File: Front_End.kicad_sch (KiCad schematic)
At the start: 40 parts, among them J6 Conn_01x03, J7 Conn_01x03, J8 Conn_01x03, J9 Conn_01x03

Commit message: Bring over ringof/dev (tranche 2, stage 1): design, library, 3D, board CI & docs
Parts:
- C48, C49, C50, C53, C54, C55, C56, C58, C59, C61: footprint TIS_Footprints:C_0603 -> Library:C_0603
- C51, C52, C57, C60: footprint TIS_Footprints:PAD_0603 -> Library:C_0603
- J6, J7, J8, J9: footprint TIS_Footprints:Pin_Header_Straight_1x03_Pitch2.54mm -> Library:Pin_Header_Straight_1x03_Pitch2.54mm
- L10, L11, L12, L13, L14, L8, L9: footprint TIS_Footprints:Murata2U -> Library:Murata2U
- R28, R29, R30, R31, R32, R33, R34, R35, R36, R37, R38, R39, R40: footprint TIS_Footprints:PAD_0603 -> Library:PAD_0603
- U12, U13: footprint TIS_Footprints:SOT-23 -> Library:SOT-23
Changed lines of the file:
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@@
 			)
 		)
-		(property "Footprint" "TIS_Footprints:PAD_0603"
+		(property "Footprint" "Library:PAD_0603"
 			(at 117.856 65.024 90)
 			(hide yes)
@@
 			)
 		)
-		(property "Footprint" "TIS_Footprints:PAD_0603"
+		(property "Footprint" "Library:C_0603"
 			(at 60.96 99.06 0)
 			(hide yes)
@@
 			)
 		)
-		(property "Footprint" "TIS_Footprints:Pin_Header_Straight_1x03_Pitch2.54mm"
+		(property "Footprint" "Library:Pin_Header_Straight_1x03_Pitch2.54mm"
 			(at 51.181 21.336 0)
 			(hide yes)
@@
 			)
 		)
-		(property "Footprint" "TIS_Footprints:PAD_0603"
+		(property "Footprint" "Library:PAD_0603"
 			(at 77.216 65.024 90)
 			(hide yes)
@@
 			)
 		)
-		(property "Footprint" "TIS_Footprints:C_0603"
+		(property "Footprint" "Library:C_0603"
 			(at 96.774 135.382 0)
 			(hide yes)
@@
 			)
 		)
-		(property "Footprint" "TIS_Footprints:Murata2U"
+		(property "Footprint" "Library:Murata2U"
 			(at 64.77 111.76 0)
 			(hide yes)
@@
 			)
 		)
-		(property "Footprint" "TIS_Footprints:Murata2U"
+		(property "Footprint" "Library:Murata2U"
 			(at 170.18 111.76 0)
 			(hide yes)
@@
 			)
 		)
-		(property "Footprint" "TIS_Footprints:C_0603"
+		(property "Footprint" "Library:C_0603"
 			(at 115.824 135.382 0)
 			(hide yes)
@@
 			)
 		)
-		(property "Footprint" "TIS_Footprints:C_0603"
+		(property "Footprint" "Library:C_0603"
 			(at 52.324 135.382 0)
 			(hide yes)
@@
 			)
 		)
-		(property "Footprint" "TIS_Footprints:PAD_0603"
+		(property "Footprint" "Library:PAD_0603"
 			(at 124.714 57.404 90)
 			(hide yes)
@@
 			)
 		)
-		(property "Footprint" "TIS_Footprints:PAD_0603"
+		(property "Footprint" "Library:PAD_0603"
 			(at 54.864 157.734 90)
 			(hide yes)
@@
 			)
 		)
-		(property "Footprint" "TIS_Footprints:PAD_0603"
+		(property "Footprint" "Library:PAD_0603"
 			(at 76.454 48.514 90)
 			(hide yes)
@@
 			)
 		)
-		(property "Footprint" "TIS_Footprints:PAD_0603"
+		(property "Footprint" "Library:PAD_0603"
 			(at 81.534 157.734 90)
 			(hide yes)
@@
 			)
 		)
-		(property "Footprint" "TIS_Footprints:C_0603"
+		(property "Footprint" "Library:C_0603"
 			(at 87.122 114.046 0)
 			(hide yes)
@@
 			)
 		)
-		(property "Footprint" "TIS_Footprints:Pin_Header_Straight_1x03_Pitch2.54mm"
+		(property "Footprint" "Library:Pin_Header_Straight_1x03_Pitch2.54mm"
 			(at 188.849 98.806 0)
 			(hide yes)
@@
 			)
 		)
-		(property "Footprint" "TIS_Footprints:PAD_0603"
+		(property "Footprint" "Library:C_0603"
 			(at 113.03 27.94 0)
 			(hide yes)
@@
 			)
 		)
-		(property "Footprint" "TIS_Footprints:C_0603"
+		(property "Footprint" "Library:C_0603"
 			(at 75.184 135.382 0)
 			(hide yes)
@@
 			)
 		)
-		(property "Footprint" "TIS_Footprints:PAD_0603"
+		(property "Footprint" "Library:PAD_0603"
 			(at 42.926 165.354 90)
 			(hide yes)
@@
 			)
 		)
-		(property "Footprint" "TIS_Footprints:Murata2U"
+		(property "Footprint" "Library:Murata2U"
 			(at 86.36 111.76 0)
 			(hide yes)
@@
 			)
 		)
-		(property "Footprint" "TIS_Footprints:SOT-23"
+		(property "Footprint" "Library:SOT-23"
 			(at 248.412 112.903 0)
 			(hide yes)
@@
 			)
 		)
-		(property "Footprint" "TIS_Footprints:C_0603"
+		(property "Footprint" "Library:C_0603"
 			(at 33.782 48.006 0)
 			(hide yes)
@@
 			)
 		)
-		(property "Footprint" "TIS_Footprints:SOT-23"
+		(property "Footprint" "Library:SOT-23"
 			(at 248.158 113.157 0)
 			(hide yes)
@@
 			)
 		)
-		(property "Footprint" "TIS_Footprints:Pin_Header_Straight_1x03_Pitch2.54mm"
+		(property "Footprint" "Library:Pin_Header_Straight_1x03_Pitch2.54mm"
 			(at 48.641 98.806 0)
 			(hide yes)
@@
 			)
 		)
-		(property "Footprint" "TIS_Footprints:PAD_0603"
+		(property "Footprint" "Library:PAD_0603"
 			(at 117.094 48.514 90)
 			(hide yes)
@@
 			)
 		)
-		(property "Footprint" "TIS_Footprints:PAD_0603"
+		(property "Footprint" "Library:PAD_0603"
 			(at 208.026 117.094 90)
 			(hide yes)
@@
 			)
 		)
-		(property "Footprint" "TIS_Footprints:C_0603"
+		(property "Footprint" "Library:C_0603"
 			(at 129.032 114.046 0)
 			(hide yes)
@@
 			)
 		)
-		(property "Footprint" "TIS_Footprints:C_0603"
+		(property "Footprint" "Library:C_0603"
 			(at 35.052 161.036 0)
 			(hide yes)
@@
 			)
 		)
-		(property "Footprint" "TIS_Footprints:C_0603"
+		(property "Footprint" "Library:C_0603"
 			(at 107.442 114.046 0)
 			(hide yes)
@@
 			)
 		)
-		(property "Footprint" "TIS_Footprints:Murata2U"
+		(property "Footprint" "Library:Murata2U"
 			(at 64.77 73.66 0)
 			(hide yes)
@@
 			)
 		)
-		(property "Footprint" "TIS_Footprints:Murata2U"
+		(property "Footprint" "Library:Murata2U"
 			(at 105.41 73.66 0)
 			(hide yes)
@@
 			)
 		)
-		(property "Footprint" "TIS_Footprints:Murata2U"
+		(property "Footprint" "Library:Murata2U"
 			(at 128.27 111.76 0)
 			(hide yes)
@@
 			)
 		)
-		(property "Footprint" "TIS_Footprints:PAD_0603"
+		(property "Footprint" "Library:C_0603"
 			(at 162.56 130.81 0)
 			(hide yes)
@@
 			)
 		)
-		(property "Footprint" "TIS_Footprints:PAD_0603"
+		(property "Footprint" "Library:PAD_0603"
 			(at 109.474 57.404 90)
 			(hide yes)
@@
 			)
 		)
-		(property "Footprint" "TIS_Footprints:Murata2U"
+		(property "Footprint" "Library:Murata2U"
 			(at 106.68 111.76 0)
 			(hide yes)
@@
 			)
 		)
-		(property "Footprint" "TIS_Footprints:PAD_0603"
+		(property "Footprint" "Library:PAD_0603"
 			(at 68.834 57.404 90)
 			(hide yes)
@@
 			)
 		)
-		(property "Footprint" "TIS_Footprints:PAD_0603"
+		(property "Footprint" "Library:PAD_0603"
 			(at 84.074 57.404 90)
 			(hide yes)
@@
 			)
 		)
-		(property "Footprint" "TIS_Footprints:PAD_0603"
+		(property "Footprint" "Library:PAD_0603"
 			(at 68.326 165.354 90)
 			(hide yes)
@@
 			)
 		)
-		(property "Footprint" "TIS_Footprints:C_0603"
+		(property "Footprint" "Library:C_0603"
 			(at 180.594 134.112 0)
 			(hide yes)
@@
 			)
 		)
-		(property "Footprint" "TIS_Footprints:PAD_0603"
+		(property "Footprint" "Library:C_0603"
 			(at 72.39 27.94 0)
 			(hide yes)
@@
 			)
 		)
-		(property "Footprint" "TIS_Footprints:Pin_Header_Straight_1x03_Pitch2.54mm"
+		(property "Footprint" "Library:Pin_Header_Straight_1x03_Pitch2.54mm"
 			(at 145.669 21.336 0)
 			(hide yes)

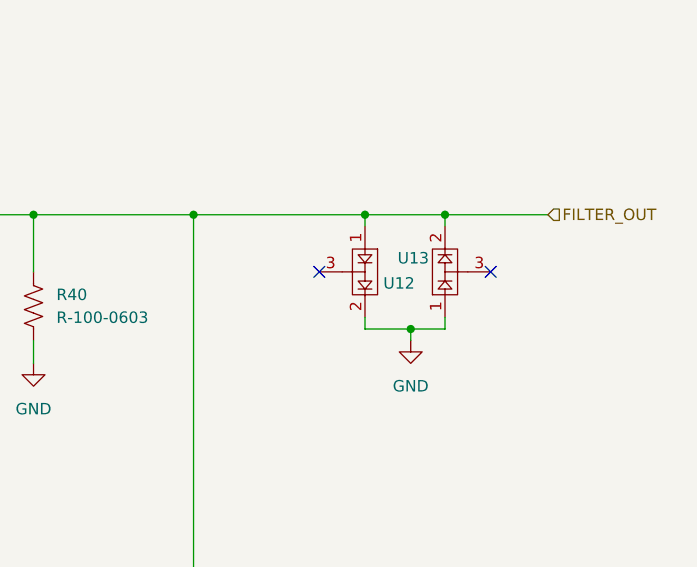
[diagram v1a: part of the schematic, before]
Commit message: fix BAV99 value, TIS exclude from BOM
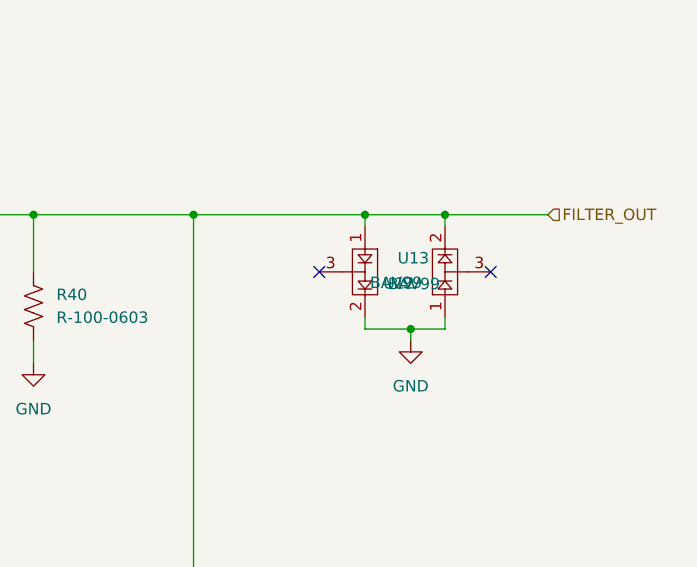
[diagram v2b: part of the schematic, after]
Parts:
- U12, U13: value (none) -> BAV99
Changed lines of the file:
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@@
 			)
 		)
-		(property "Value" ""
+		(property "Value" "BAV99"
 			(at 246.38 114.3635 90)
 			(show_name no)
@@
 			)
 		)
-		(property "Value" ""
+		(property "Value" "BAV99"
 			(at 250.19 114.2365 90)
 			(show_name no)

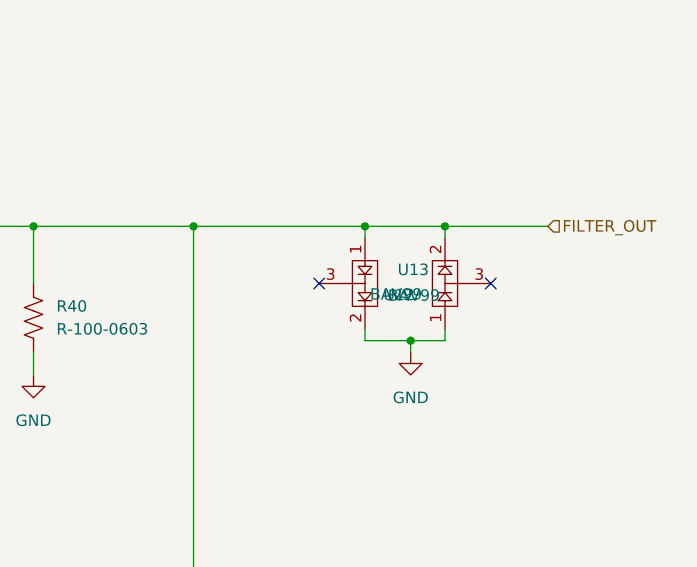
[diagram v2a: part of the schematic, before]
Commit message: Reconcile library/schematic/board drift (ERC/DRC clean at full severity)
Full-severity ERC/DRC surfaced 22 lib_symbol_mismatch + 5 lib_footprint_mismatch
warnings from cached copies drifting off the library master. Reconciled and
verified against the schematic and board:

- Symbol caches: refresh 8 cap/diode symbols whose embedded footprint field was
  stale (PAD_0603 -> C_0603); instances and PCB already used C_0603.
- SMA (J1-J4): push the board's tuned 3D-model offset/rotate into the library
  master and re-save it in KiCad 10 format; fix J1 LCSC C2874826 -> C914558 in
  schematic and board (J1 was an error, not a variant).
- U.FL (J10): re-save library footprint in v10 to match the routed board.

Result: ERC 0, DRC 0 (errors + warnings).
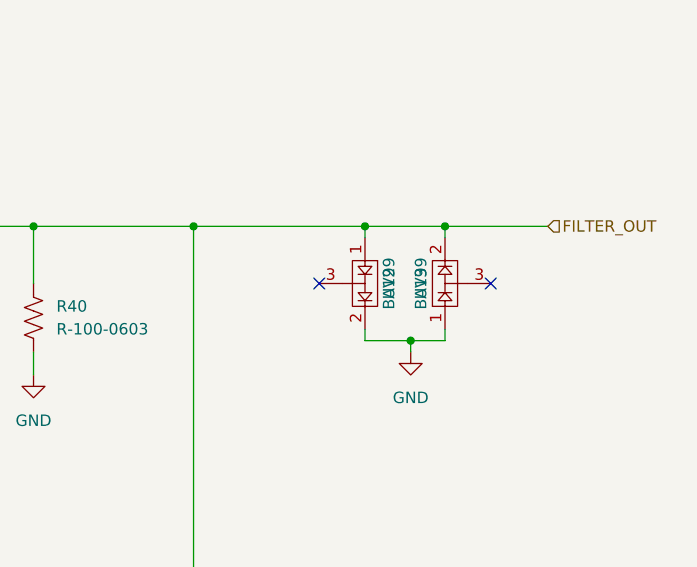
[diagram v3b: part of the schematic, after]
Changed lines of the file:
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@@
 		(dnp no)
 		(property "Reference" "U12"
-			(at 245.872 114.3 90)
+			(at 246.507 113.03 0)
 			(show_name no)
 			(do_not_autoplace no)
@@
 					(size 1.27 1.27)
 				)
-				(justify left)
 			)
 		)
 		(property "Value" "BAV99"
-			(at 246.38 114.3635 90)
+			(at 246.507 113.03 0)
 			(show_name no)
 			(do_not_autoplace no)
@@
 					(size 1.27 1.27)
 				)
-				(justify left)
 			)
 		)
@@
 		(dnp no)
 		(property "Reference" "U13"
-			(at 250.952 111.506 90)
+			(at 250.063 113.03 0)
 			(show_name no)
 			(do_not_autoplace no)
@@
 					(size 1.27 1.27)
 				)
-				(justify left)
 			)
 		)
 		(property "Value" "BAV99"
-			(at 250.19 114.2365 90)
+			(at 250.063 113.03 0)
 			(show_name no)
 			(do_not_autoplace no)
@@
 					(size 1.27 1.27)
 				)
-				(justify left)
 			)
 		)

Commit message: reselect L10/L11 120 nH to LCSC C703706 Murata 2% variant (was 5% variant) as original is no longer stocked
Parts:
- L10, L11: LCSC Part # C2044072 -> C703706
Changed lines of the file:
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@@
 			)
 		)
-		(property "LCSC Part #" "C2044072"
+		(property "LCSC Part #" "C703706"
 			(at 86.487 113.538 0)
 			(hide yes)
@@
 			)
 		)
-		(property "LCSC Part #" "C2044072"
+		(property "LCSC Part #" "C703706"
 			(at 106.807 113.538 0)
 			(hide yes)
